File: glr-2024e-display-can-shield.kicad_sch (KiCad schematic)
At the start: 10 parts, among them CN6 Conn_01x08, CN8 Conn_01x06, IC1 L9615D013TR, J3 Conn_02x08_Odd_Even, J4 Screw_Terminal_01x12

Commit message: add initial pcb layout
Co-Authored-By: wallalex0 <97884125+wallalex0@users.noreply.github.com>
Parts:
- added J2: Screw_Terminal_01x08, symbol Connector:Screw_Terminal_01x08
- added J3: Screw_Terminal_01x04, symbol Connector:Screw_Terminal_01x04
- C1: footprint (none) -> Capacitor_SMD:C_0201_0603Metric
- CN12: renamed from J3; footprint (none) -> Connector_PinSocket_2.54mm:PinSocket_2x08_P2.54mm_Vertical
- CN6: footprint (none) -> Connector_PinHeader_2.54mm:PinHeader_1x08_P2.54mm_Vertical
- CN8: footprint (none) -> Connector_PinHeader_2.54mm:PinHeader_1x06_P2.54mm_Vertical
- D1: footprint (none) -> Diode_SMD:D_0201_0603Metric
- J1: renamed from J4; footprint (none) -> TerminalBlock_Altech:Altech_AK100_1x12_P5.00mm
- R1, R2: footprint (none) -> Resistor_SMD:R_0201_0603Metric
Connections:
- net +3V3: no longer names the net of CN6.4 (Pin_4)
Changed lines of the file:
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@@
+	(wire
+		(pts
+			(xy 107.95 87.63) (xy 107.95 110.49)
+		)
+		(stroke
+			(width 0)
+			(type default)
+		)
+	)
 	(wire
 		(pts
@@
 	(wire
 		(pts
-			(xy 107.95 87.63) (xy 107.95 110.49)
-		)
-		(stroke
-			(width 0)
-			(type default)
-		)
-	)
-	(wire
-		(pts
 			(xy 125.73 87.63) (xy 107.95 87.63)
 		)
@@
 	(wire
 		(pts
-			(xy 74.93 53.34) (xy 80.01 53.34)
+			(xy 96.52 77.47) (xy 96.52 127)
 		)
 		(stroke
@@
 		(pts
 			(xy 90.17 76.2) (xy 74.93 76.2)
-		)
-		(stroke
-			(width 0)
-			(type default)
-		)
-	)
-	(wire
-		(pts
-			(xy 96.52 77.47) (xy 96.52 127)
 		)
 		(stroke
@@
 	)
 	(label "Tx"
-		(at 96.52 116.84 0)
+		(at 96.52 107.95 0)
 		(effects
 			(font
@@
 	)
 	(label "Rx"
-		(at 107.95 110.49 0)
+		(at 107.95 107.95 0)
 		(effects
 			(font
@@
 			)
 		)
-		(property "Footprint" ""
+		(property "Footprint" "Capacitor_SMD:C_0201_0603Metric"
 			(at 110.49 82.55 0)
 			(effects
@@
 	)
 	(symbol
+		(lib_id "Connector:Screw_Terminal_01x04")
+		(at 204.47 92.71 0)
+		(unit 1)
+		(exclude_from_sim no)
+		(in_bom yes)
+		(on_board yes)
+		(dnp no)
+		(fields_autoplaced yes)
+		(property "Reference" "J3"
+			(at 207.01 92.7099 0)
+			(effects
+				(font
+					(size 1.27 1.27)
+				)
+				(justify left)
+			)
+		)
+		(property "Value" "Screw_Terminal_01x04"
+			(at 207.01 95.2499 0)
+			(effects
+				(font
+					(size 1.27 1.27)
+				)
+				(justify left)
+			)
+		)
+		(property "Footprint" ""
+			(at 204.47 92.71 0)
+			(effects
+				(font
+					(size 1.27 1.27)
+				)
+				(hide yes)
+			)
+		)
+		(property "Datasheet" "~"
+			(at 204.47 92.71 0)
+			(effects
+				(font
+					(size 1.27 1.27)
+				)
+				(hide yes)
+			)
+		)
+		(property "Description" "Generic screw terminal, single row, 01x04, script generated (kicad-library-utils/schlib/autogen/connector/)"
+			(at 204.47 92.71 0)
+			(effects
+				(font
+					(size 1.27 1.27)
+				)
+				(hide yes)
+			)
+		)
+		(pin "3"
+		)
+		(pin "1"
+		)
+		(pin "2"
+		)
+		(pin "4"
+		)
+		(instances
+			(project ""
+				(path "/3ec1d028-83c5-460a-a6b1-0c7e981bb79c"
+					(reference "J3")
+					(unit 1)
+				)
+			)
+		)
+	)
+	(symbol
 		(lib_id "Connector:Screw_Terminal_01x12")
 		(at 187.96 138.43 0)
@@
 		(dnp no)
 		(fields_autoplaced yes)
-		(property "Reference" "J4"
+		(property "Reference" "J1"
 			(at 190.5 138.4299 0)
 			(effects
@@
 			)
 		)
-		(property "Footprint" ""
+		(property "Footprint" "TerminalBlock_Altech:Altech_AK100_1x12_P5.00mm"
 			(at 187.96 138.43 0)
 			(effects
@@
 			(project ""
 				(path "/3ec1d028-83c5-460a-a6b1-0c7e981bb79c"
-					(reference "J4")
+					(reference "J1")
 					(unit 1)
 				)
@@
 			)
 		)
-		(property "Footprint" ""
+		(property "Footprint" "Resistor_SMD:R_0201_0603Metric"
 			(at 163.83 93.218 90)
 			(effects
@@
 			)
 		)
-		(property "Footprint" ""
+		(property "Footprint" "Diode_SMD:D_0201_0603Metric"
 			(at 175.26 125.73 0)
 			(effects
@@
 				(path "/3ec1d028-83c5-460a-a6b1-0c7e981bb79c"
 					(reference "D1")
-					(unit 1)
-				)
-			)
-		)
-	)
-	(symbol
-		(lib_id "power:+3V3")
-		(at 80.01 53.34 270)
-		(unit 1)
-		(exclude_from_sim no)
-		(in_bom yes)
-		(on_board yes)
-		(dnp no)
-		(fields_autoplaced yes)
-		(property "Reference" "#PWR02"
-			(at 76.2 53.34 0)
-			(effects
-				(font
-					(size 1.27 1.27)
-				)
-				(hide yes)
-			)
-		)
-		(property "Value" "+3V3"
-			(at 83.82 53.3399 90)
-			(effects
-				(font
-					(size 1.27 1.27)
-				)
-				(justify left)
-			)
-		)
-		(property "Footprint" ""
-			(at 80.01 53.34 0)
-			(effects
-				(font
-					(size 1.27 1.27)
-				)
-				(hide yes)
-			)
-		)
-		(property "Datasheet" ""
-			(at 80.01 53.34 0)
-			(effects
-				(font
-					(size 1.27 1.27)
-				)
-				(hide yes)
-			)
-		)
-		(property "Description" "Power symbol creates a global label with name \"+3V3\""
-			(at 80.01 53.34 0)
-			(effects
-				(font
-					(size 1.27 1.27)
-				)
-				(hide yes)
-			)
-		)
-		(pin "1"
-		)
-		(instances
-			(project ""
-				(path "/3ec1d028-83c5-460a-a6b1-0c7e981bb79c"
-					(reference "#PWR02")
 					(unit 1)
 				)
@@
 			)
 		)
-		(property "Footprint" ""
+		(property "Footprint" "Connector_PinHeader_2.54mm:PinHeader_1x06_P2.54mm_Vertical"
 			(at 69.85 81.28 0)
 			(effects
@@
 		(on_board yes)
 		(dnp no)
-		(fields_autoplaced yes)
-		(property "Reference" "J3"
-			(at 124.46 116.84 0)
-			(effects
-				(font
-					(size 1.27 1.27)
-				)
+		(property "Reference" "CN12"
+			(at 120.142 115.316 90)
+			(effects
+				(font
+					(size 1.27 1.27)
+				)
+				(justify left)
 			)
 		)
 		(property "Value" "Conn_02x08_Odd_Even"
-			(at 121.92 116.84 0)
-			(effects
-				(font
-					(size 1.27 1.27)
-				)
-			)
-		)
-		(property "Footprint" ""
+			(at 141.986 117.602 90)
+			(effects
+				(font
+					(size 1.27 1.27)
+				)
+				(justify right)
+			)
+		)
+		(property "Footprint" "Connector_PinSocket_2.54mm:PinSocket_2x08_P2.54mm_Vertical"
 			(at 110.49 115.57 0)
 			(effects
@@
 			(project ""
 				(path "/3ec1d028-83c5-460a-a6b1-0c7e981bb79c"
-					(reference "J3")
+					(reference "CN12")
 					(unit 1)
 				)
@@
 			)
 		)
-		(property "Footprint" ""
+		(property "Footprint" "Connector_PinHeader_2.54mm:PinHeader_1x08_P2.54mm_Vertical"
 			(at 69.85 53.34 0)
 			(effects
@@
 			)
 		)
-		(property "Footprint" ""
+		(property "Footprint" "Resistor_SMD:R_0201_0603Metric"
 			(at 173.99 93.218 90)
 			(effects
@@
 					(unit 1)
 				)
+			)
+		)
+	)
+	(symbol
+		(lib_id "Connector:Screw_Terminal_01x08")
+		(at 210.82 111.76 0)
+		(unit 1)
+		(exclude_from_sim no)
+		(in_bom yes)
+		(on_board yes)
+		(dnp no)
+		(fields_autoplaced yes)
+		(property "Reference" "J2"
+			(at 213.36 111.7599 0)
+			(effects
+				(font
+					(size 1.27 1.27)
+				)
+				(justify left)
+			)
+		)
+		(property "Value" "Screw_Terminal_01x08"
+			(at 213.36 114.2999 0)
+			(effects
+				(font
+					(size 1.27 1.27)
+				)
+				(justify left)
+			)
+		)
+		(property "Footprint" ""
+			(at 210.82 111.76 0)
+			(effects
+				(font
+					(size 1.27 1.27)
+				)
+				(hide yes)
+			)
+		)
+		(property "Datasheet" "~"
+			(at 210.82 111.76 0)
+			(effects
+				(font
+					(size 1.27 1.27)
+				)
+				(hide yes)
+			)
+		)
+		(property "Description" "Generic screw terminal, single row, 01x08, script generated (kicad-library-utils/schlib/autogen/connector/)"
+			(at 210.82 111.76 0)
+			(effects
+				(font
+					(size 1.27 1.27)
+				)
+				(hide yes)
+			)
+		)
+		(pin "1"
+		)
+		(pin "3"
+		)
+		(pin "7"
+		)
+		(pin "4"
+		)
+		(pin "5"
+		)
+		(pin "8"
+		)
+		(pin "2"
+		)
+		(pin "6"
+		)
+		(instances
+			(project ""
+				(path "/3ec1d028-83c5-460a-a6b1-0c7e981bb79c"
+					(reference "J2")
+					(unit 1)
+				)

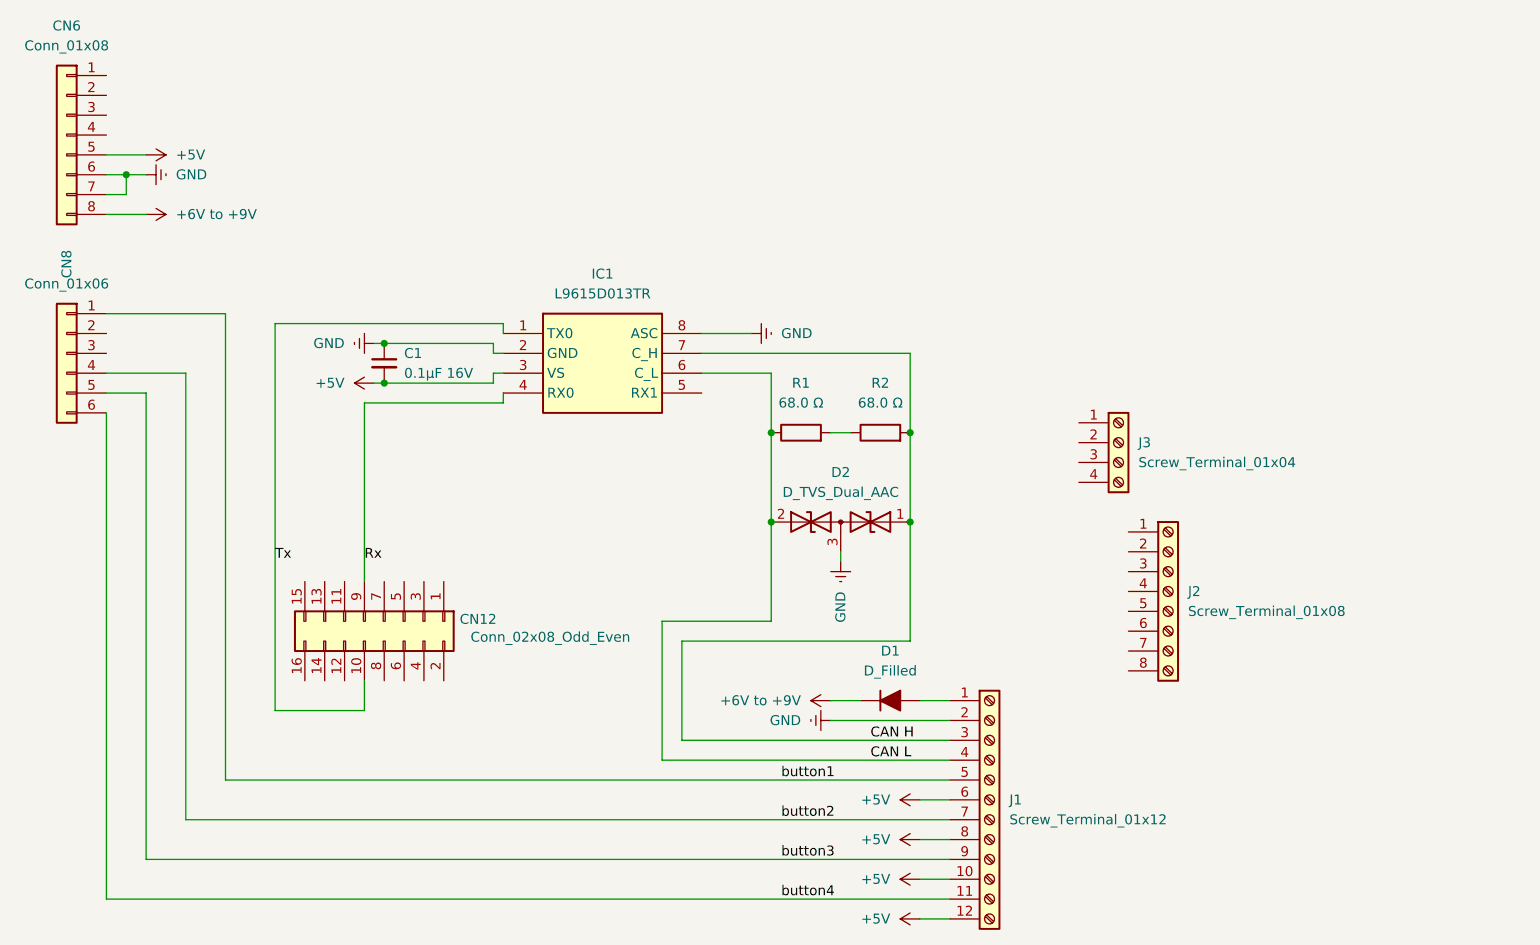
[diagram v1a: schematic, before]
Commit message: make 4pin and 8pin screw terminal instead of 12pin
use exact footprint and 3d model

Co-Authored-By: wallalex0 <97884125+wallalex0@users.noreply.github.com>
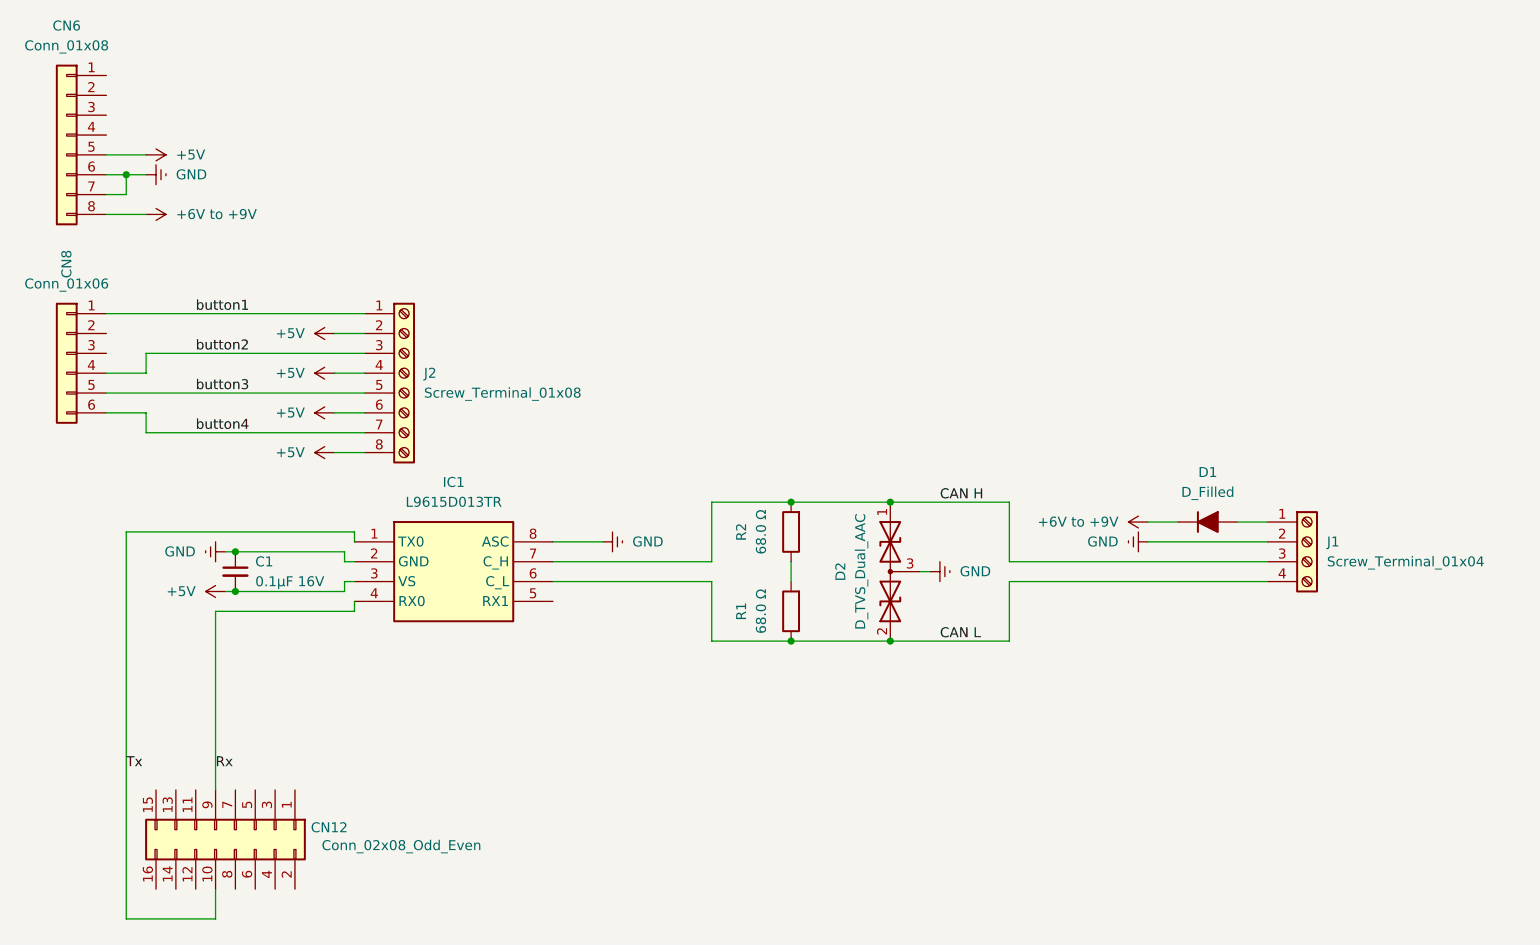
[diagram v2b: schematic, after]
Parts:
- removed J1: Screw_Terminal_01x12, TerminalBlock_Altech:Altech_AK100_1x12_P5.00mm, symbol Connector:Screw_Terminal_01x12
- J1: renamed from J3; footprint (none) -> GLR_KiCAD_Library:WECO-950-FB-04
- J2: footprint (none) -> GLR_KiCAD_Library:WECO-950-FB-08
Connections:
- net +5V: now also J2.2 (Pin_2), J2.4 (Pin_4), J2.6 (Pin_6), J2.8 (Pin_8)
- net CAN H: now also J1.3 (Pin_3)
- net CAN L: now also J1.4 (Pin_4)
- net GND: now also J1.2 (Pin_2)
- net button1: now also J2.1 (Pin_1)
- net button2: now also J2.3 (Pin_3)
- net button3: now also J2.5 (Pin_5)
- net button4: now also J2.7 (Pin_7)
- net at J1.1 (Pin_1): now also D1.2 (A)
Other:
- moved on the sheet: C1, CN12, D1, D2, IC1, J1, J2, R1, R2

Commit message: add voltage regulator 12V -> 8V
improve alignment of connectors
add board outline
add descriptions

Co-Authored-By: wallalex0 <97884125+wallalex0@users.noreply.github.com>
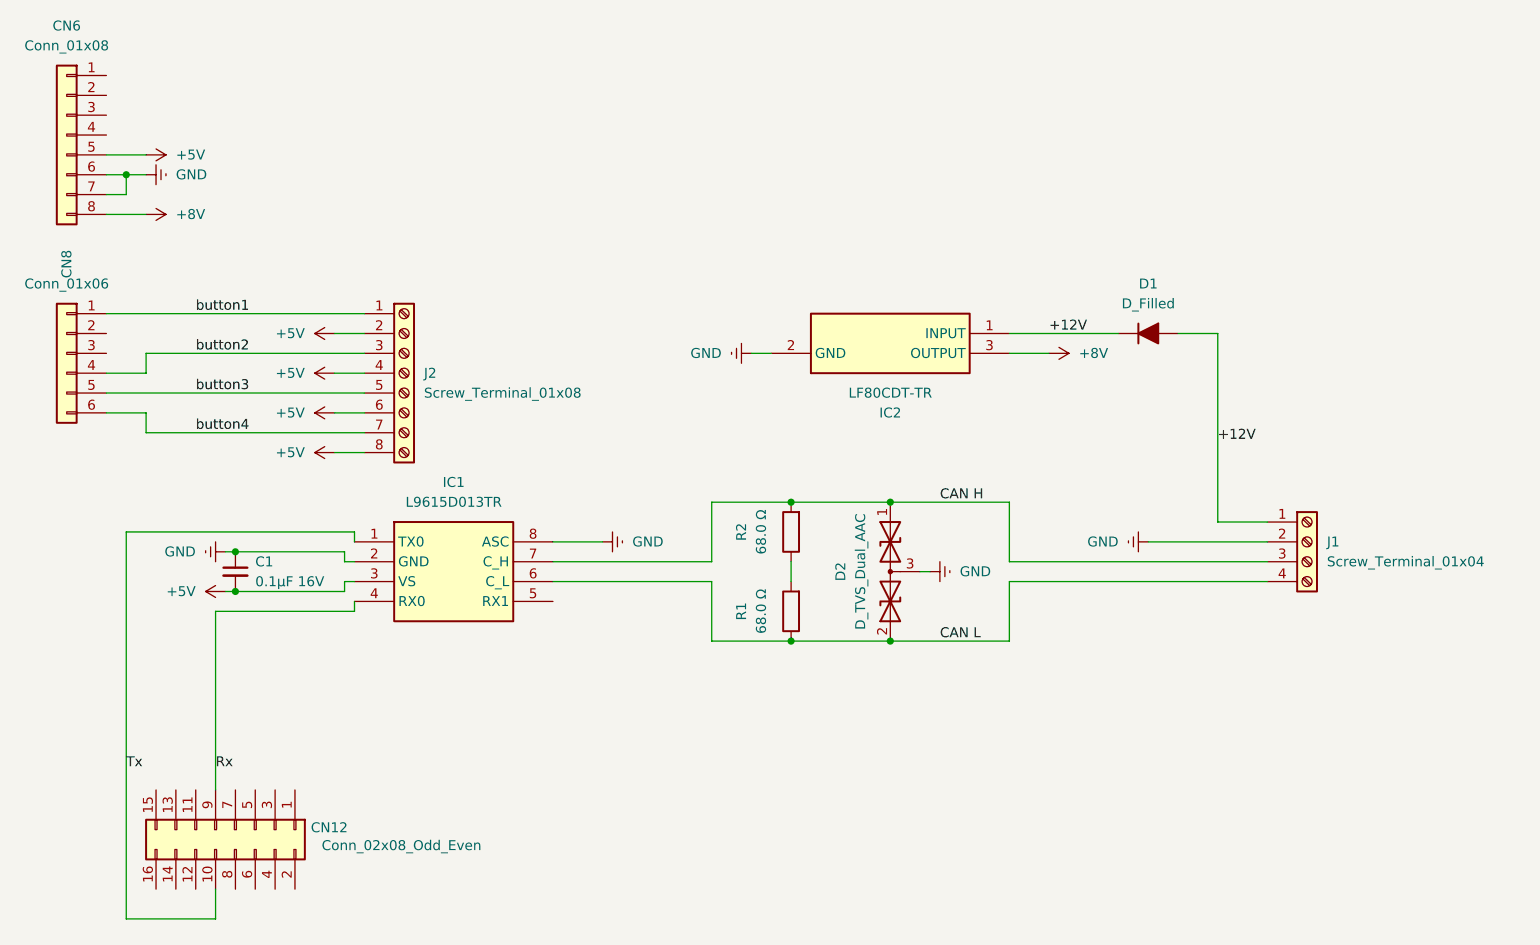
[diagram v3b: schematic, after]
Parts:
- added IC2: LF80CDT-TR, LF80CDTTR, symbol SamacSys_Parts:LF80CDT-TR
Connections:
- net GND: now also IC2.2 (GND)
- net +12V: now reaches D1.2 (A), J1.1 (Pin_1)
- net +12V: now also D1.1 (K), IC2.1 (INPUT)
- net +6V to +9V renamed +8V
- net +8V: now also IC2.3 (OUTPUT); no longer D1.1 (K)
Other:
- moved on the sheet: D1

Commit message: explicitly define which parts to use
Co-Authored-By: wallalex0 <97884125+wallalex0@users.noreply.github.com>
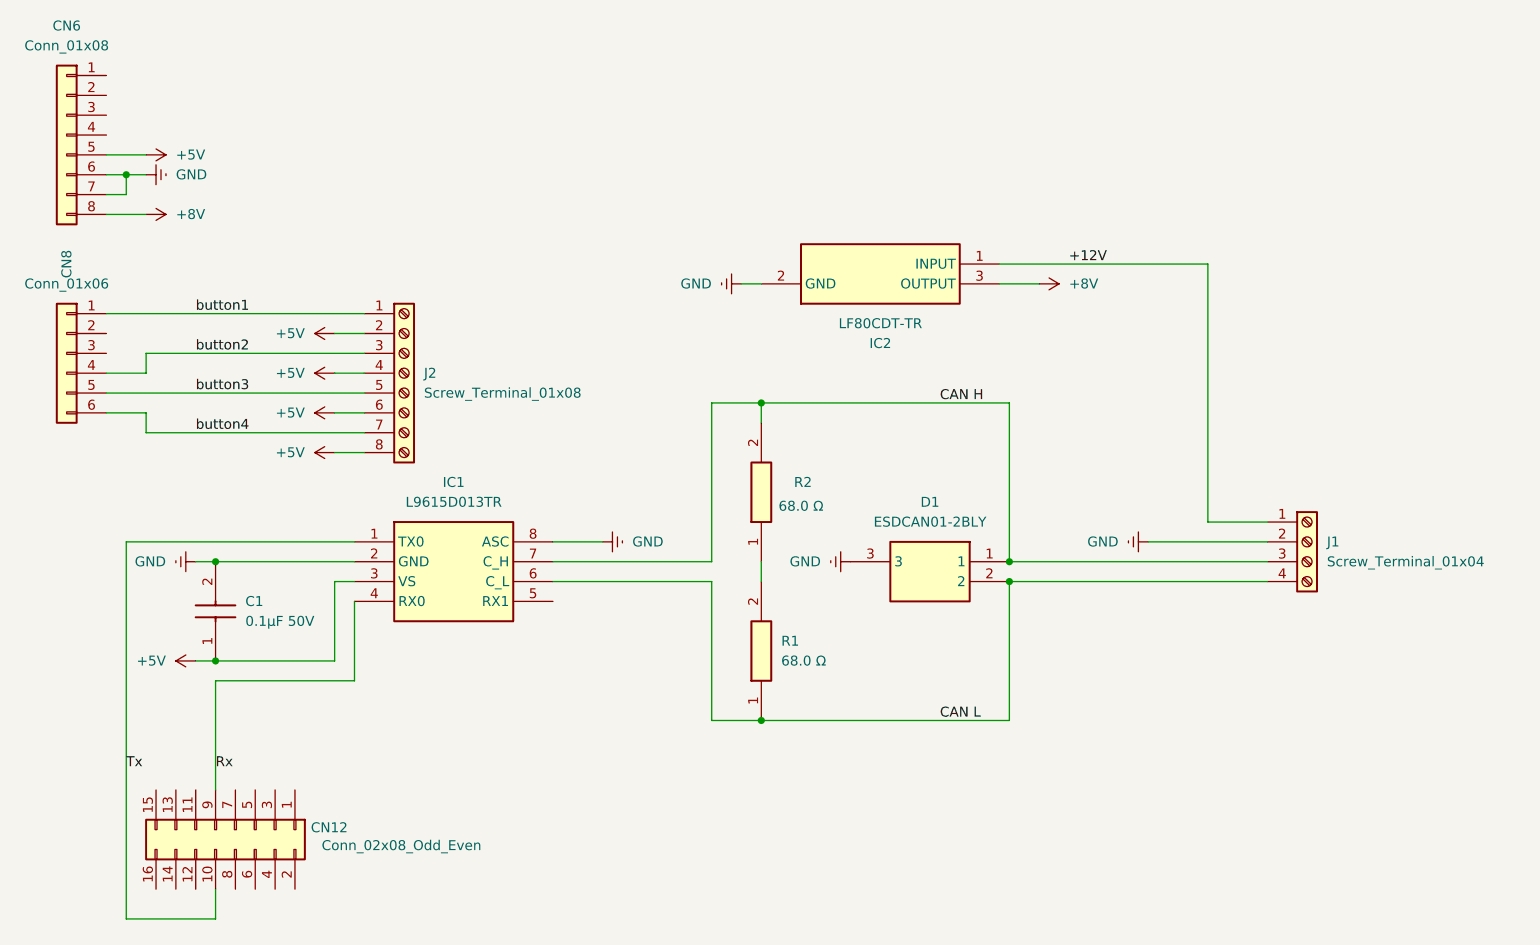
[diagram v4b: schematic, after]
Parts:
- removed D1: D_Filled, Diode_SMD:D_0201_0603Metric, symbol Device:D_Filled
- C1: value 0.1μF 16V -> 0.1μF 50V; footprint Capacitor_SMD:C_0201_0603Metric -> CAPC1608X90N; symbol Device:C_Small -> SamacSys_Parts:CL10B104KB8NNNC; Height (none) -> 0.9; Manufacturer_Name (none) -> SAMSUNG; Manufacturer_Part_Number (none) -> CL10B104KB8NNNC
- D1: renamed from D2; value D_TVS_Dual_AAC -> ESDCAN01-2BLY; footprint Package_TO_SOT_SMD:SOT-23 -> SOT95P255X125-3N; symbol Device:D_TVS_Dual_AAC -> SamacSys_Parts:ESDCAN01-2BLY; Height (none) -> 1.25; Manufacturer_Name (none) -> STMicroelectronics; Manufacturer_Part_Number (none) -> ESDCAN01-2BLY; Mouser Part Number (none) -> 511-ESDCAN01-2BLY; Mouser Price/Stock (none) -> https://www.mouser.co.uk/ProductDetail/STMicroelectronics/E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
- R1, R2: footprint Resistor_SMD:R_0201_0603Metric -> RESC1608X50N; symbol Device:R -> SamacSys_Parts:CRCW060368R1FKEA; Height (none) -> 0.5; Manufacturer_Name (none) -> Vishay; Manufacturer_Part_Number (none) -> CRCW060368R1FKEA
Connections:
- net +5V: now also C1.1; no longer C1.2
- net GND: now also C1.2; no longer C1.1
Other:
- moved on the sheet: IC2
